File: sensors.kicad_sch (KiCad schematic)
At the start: 10 parts, among them J12 GND, J13 Sensor, J14 3.3v, J15 SDA, J16 SCL, U33 BMI270

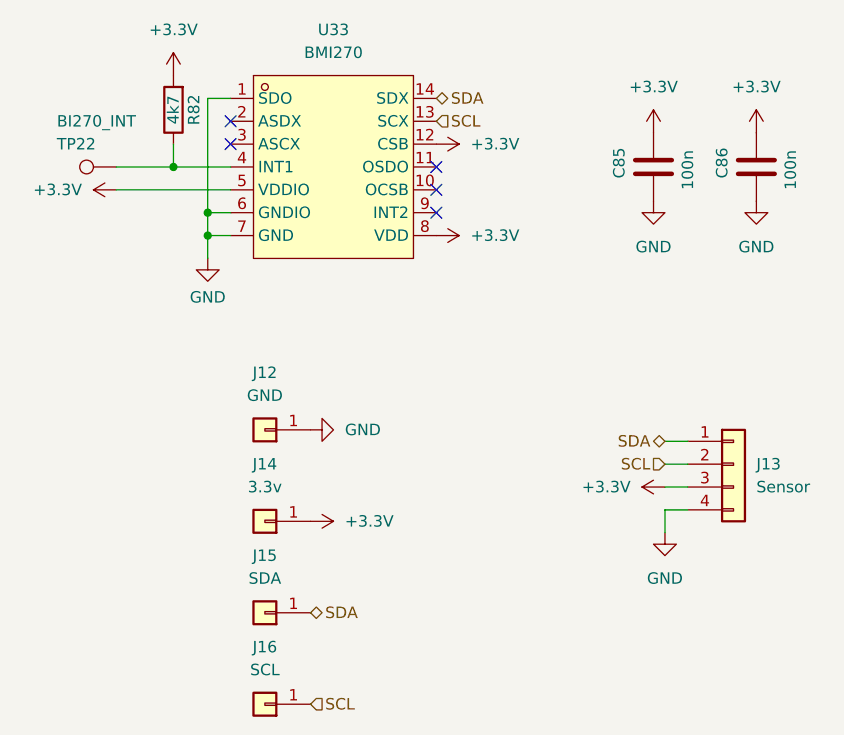
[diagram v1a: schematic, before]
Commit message: Revision 7 (#18)
* Revision 7: fix SD card power control circuit

* Add missing LCSC SKU
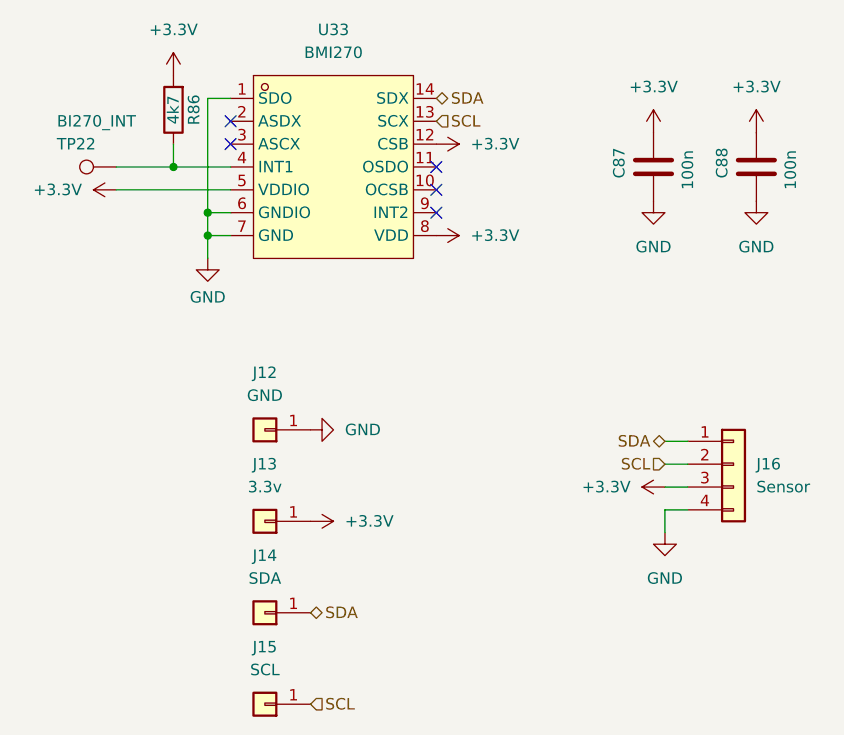
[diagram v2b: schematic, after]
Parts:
- renumbered C85 to C87, C86 to C88, J14 to J13, J15 to J14, J16 to J15, J13 to J16, R82 to R86
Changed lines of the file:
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@@
 	(title_block
 		(title "Tanmatsu")
-		(date "2025-12-12")
-		(rev "6")
+		(date "2026-02-04")
+		(rev "7")
 		(company "Nicolai Electronics")
-		(comment 1 "Copyright 2025 Paul Honig")
-		(comment 2 "Copyright 2025 Nicolai Electronics")
+		(comment 1 "Copyright 2026 Paul Honig")
+		(comment 2 "Copyright 2026 Nicolai Electronics")
 		(comment 3 "License: CERN-OHL-P")
 	)
@@
 		(dnp no)
 		(fields_autoplaced yes)
-		(property "Reference" "#PWR0299"
+		(property "Reference" "#PWR0298"
 			(at 45.72 73.66 0)
 			(effects
@@
 			(project "why2025"
 				(path "/6a31734e-65de-48f3-8156-2b24b665b183/14d9c0ee-00ab-4a1b-b059-e8045c71d6ae"
-					(reference "#PWR0299")
+					(reference "#PWR0298")
 					(unit 1)
 				)
@@
 		(on_board yes)
 		(dnp no)
-		(property "Reference" "#PWR0293"
+		(property "Reference" "#PWR0302"
 			(at 87.63 44.45 0)
 			(effects
@@
 			(project "why2025"
 				(path "/6a31734e-65de-48f3-8156-2b24b665b183/14d9c0ee-00ab-4a1b-b059-e8045c71d6ae"
-					(reference "#PWR0293")
+					(reference "#PWR0302")
 					(unit 1)
 				)
@@
 		(dnp no)
 		(fields_autoplaced yes)
-		(property "Reference" "J14"
+		(property "Reference" "J13"
 			(at 44.45 67.31 0)
 			(effects
@@
 			(project "why2025"
 				(path "/6a31734e-65de-48f3-8156-2b24b665b183/14d9c0ee-00ab-4a1b-b059-e8045c71d6ae"
-					(reference "J14")
+					(reference "J13")
 					(unit 1)
 				)
@@
 		(dnp no)
 		(fields_autoplaced yes)
-		(property "Reference" "#PWR0295"
+		(property "Reference" "#PWR0300"
 			(at 59.69 41.91 0)
 			(effects
@@
 			(project "why2025"
 				(path "/6a31734e-65de-48f3-8156-2b24b665b183/14d9c0ee-00ab-4a1b-b059-e8045c71d6ae"
-					(reference "#PWR0295")
+					(reference "#PWR0300")
 					(unit 1)
 				)
@@
 		(dnp no)
 		(fields_autoplaced yes)
-		(property "Reference" "#PWR0291"
+		(property "Reference" "#PWR0299"
 			(at 59.69 31.75 0)
 			(effects
@@
 			(project "why2025"
 				(path "/6a31734e-65de-48f3-8156-2b24b665b183/14d9c0ee-00ab-4a1b-b059-e8045c71d6ae"
-					(reference "#PWR0291")
+					(reference "#PWR0299")
 					(unit 1)
 				)
@@
 		(on_board yes)
 		(dnp no)
-		(property "Reference" "C85"
+		(property "Reference" "C87"
 			(at 83.82 35.56 90)
 			(effects
@@
 			(project "why2025"
 				(path "/6a31734e-65de-48f3-8156-2b24b665b183/14d9c0ee-00ab-4a1b-b059-e8045c71d6ae"
-					(reference "C85")
+					(reference "C87")
 					(unit 1)
 				)
@@
 		(dnp no)
 		(fields_autoplaced yes)
-		(property "Reference" "#PWR0289"
+		(property "Reference" "#PWR0301"
 			(at 87.63 34.29 0)
 			(effects
@@
 			(project "why2025"
 				(path "/6a31734e-65de-48f3-8156-2b24b665b183/14d9c0ee-00ab-4a1b-b059-e8045c71d6ae"
-					(reference "#PWR0289")
+					(reference "#PWR0301")
 					(unit 1)
 				)
@@
 		(dnp no)
 		(fields_autoplaced yes)
-		(property "Reference" "J13"
+		(property "Reference" "J16"
 			(at 99.06 67.3099 0)
 			(effects
@@
 			(project ""
 				(path "/6a31734e-65de-48f3-8156-2b24b665b183/14d9c0ee-00ab-4a1b-b059-e8045c71d6ae"
-					(reference "J13")
+					(reference "J16")
 					(unit 1)
 				)
@@
 		(dnp no)
 		(fields_autoplaced yes)
-		(property "Reference" "#PWR0290"
+		(property "Reference" "#PWR0305"
 			(at 99.06 34.29 0)
 			(effects
@@
 			(project "why2025"
 				(path "/6a31734e-65de-48f3-8156-2b24b665b183/14d9c0ee-00ab-4a1b-b059-e8045c71d6ae"
-					(reference "#PWR0290")
+					(reference "#PWR0305")
 					(unit 1)
 				)
@@
 		(dnp no)
 		(fields_autoplaced yes)
-		(property "Reference" "#PWR0298"
+		(property "Reference" "#PWR0303"
 			(at 92.71 69.85 0)
 			(effects
@@
 			(project "tanmatsu"
 				(path "/6a31734e-65de-48f3-8156-2b24b665b183/14d9c0ee-00ab-4a1b-b059-e8045c71d6ae"
-					(reference "#PWR0298")
+					(reference "#PWR0303")
 					(unit 1)
 				)
@@
 		(dnp no)
 		(fields_autoplaced yes)
-		(property "Reference" "J16"
+		(property "Reference" "J15"
 			(at 44.45 87.63 0)
 			(effects
@@
 			(project "why2025"
 				(path "/6a31734e-65de-48f3-8156-2b24b665b183/14d9c0ee-00ab-4a1b-b059-e8045c71d6ae"
-					(reference "J16")
+					(reference "J15")
 					(unit 1)
 				)
@@
 		(dnp no)
 		(fields_autoplaced yes)
-		(property "Reference" "#PWR0292"
+		(property "Reference" "#PWR0294"
 			(at 31.75 36.83 0)
 			(effects
@@
 			(project "why2025"
 				(path "/6a31734e-65de-48f3-8156-2b24b665b183/14d9c0ee-00ab-4a1b-b059-e8045c71d6ae"
-					(reference "#PWR0292")
+					(reference "#PWR0294")
 					(unit 1)
 				)
@@
 		(dnp no)
 		(fields_autoplaced yes)
-		(property "Reference" "#PWR0300"
+		(property "Reference" "#PWR0304"
 			(at 88.9 81.28 0)
 			(effects
@@
 			(project "tanmatsu"
 				(path "/6a31734e-65de-48f3-8156-2b24b665b183/14d9c0ee-00ab-4a1b-b059-e8045c71d6ae"
-					(reference "#PWR0300")
+					(reference "#PWR0304")
 					(unit 1)
 				)
@@
 		(on_board yes)
 		(dnp no)
-		(property "Reference" "#PWR0294"
+		(property "Reference" "#PWR0306"
 			(at 99.06 44.45 0)
 			(effects
@@
 			(project "why2025"
 				(path "/6a31734e-65de-48f3-8156-2b24b665b183/14d9c0ee-00ab-4a1b-b059-e8045c71d6ae"
-					(reference "#PWR0294")
+					(reference "#PWR0306")
 					(unit 1)
 				)
@@
 		(on_board yes)
 		(dnp no)
-		(property "Reference" "R82"
+		(property "Reference" "R86"
 			(at 36.576 27.94 90)
 			(effects
@@
 			(project "why2025"
 				(path "/6a31734e-65de-48f3-8156-2b24b665b183/14d9c0ee-00ab-4a1b-b059-e8045c71d6ae"
-					(reference "R82")
+					(reference "R86")
 					(unit 1)
 				)
@@
 		(dnp no)
 		(fields_autoplaced yes)
-		(property "Reference" "J15"
+		(property "Reference" "J14"
 			(at 44.45 77.47 0)
 			(effects
@@
 			(project "why2025"
 				(path "/6a31734e-65de-48f3-8156-2b24b665b183/14d9c0ee-00ab-4a1b-b059-e8045c71d6ae"
-					(reference "J15")
+					(reference "J14")
 					(unit 1)
 				)
@@
 		(dnp no)
 		(fields_autoplaced yes)
-		(property "Reference" "#PWR0288"
+		(property "Reference" "#PWR0295"
 			(at 34.29 27.94 0)
 			(effects
@@
 			(project "why2025"
 				(path "/6a31734e-65de-48f3-8156-2b24b665b183/14d9c0ee-00ab-4a1b-b059-e8045c71d6ae"
-					(reference "#PWR0288")
+					(reference "#PWR0295")
 					(unit 1)
 				)
@@
 		(on_board yes)
 		(dnp no)
-		(property "Reference" "C86"
+		(property "Reference" "C88"
 			(at 95.25 35.56 90)
 			(effects
@@
 			(project "why2025"
 				(path "/6a31734e-65de-48f3-8156-2b24b665b183/14d9c0ee-00ab-4a1b-b059-e8045c71d6ae"
-					(reference "C86")
-					(unit 1)
-				)
+					(reference "C88")
+					(unit 1)
+				)
